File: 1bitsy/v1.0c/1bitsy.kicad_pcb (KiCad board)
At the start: 4 copper layers, 38.1 x 17.8 mm, 105 parts, among them J1 BOOT, P1 CONN_01X01, P10 CONN_01X01, P11 CONN_01X01, P12 CONN_01X01, P13 CONN_01X01, P14 CONN_01X01, P15 CONN_01X01, P16 CONN_01X01, P17 CONN_01X01, P18 CONN_01X01, P19 CONN_01X01, P2 CONN_01X01, P20 CONN_01X01, P21 CONN_01X01, P22 CONN_01X01, P23 CONN_01X01, P24 USB_OTG, P25 CONN_01X01, P26 CONN_01X01, P27 CONN_01X01, P28 CONN_01X01, P29 CONN_01X01, P3 CONN_01X01, P30 CONN_01X01, P31 CONN_01X01, P32 CONN_01X01, P33 CONN_01X01, P34 CONN_01X01, P35 CONN_01X01, P36 CONN_01X01, P37 CONN_01X01, P38 CONN_01X01, P39 CONN_01X01, P4 CONN_01X01, P40 CONN_01X01, P41 CONN_01X01, P42 CONN_01X01, P43 TP, P44 TP, P45 TP, P46 TP, P47 TP, P48 CONN_01X01, P49 CONN_01X01, P5 CONN_01X01, P50 CONN_01X01, P51 CONN_01X01, P52 CONN_01X01, P53 CONN_01X01, P54 CONN_01X01, P55 CONN_01X01, P6 CONN_01X01, P7 CONN_01X01, P8 CONN_01X01, P9 CONN_01X01, SW1 TACT_G, U1 VREG_3V3, U2 STM32F415RGT, X1 32.768kHz, X2 25MHz, X3 JTAG-10

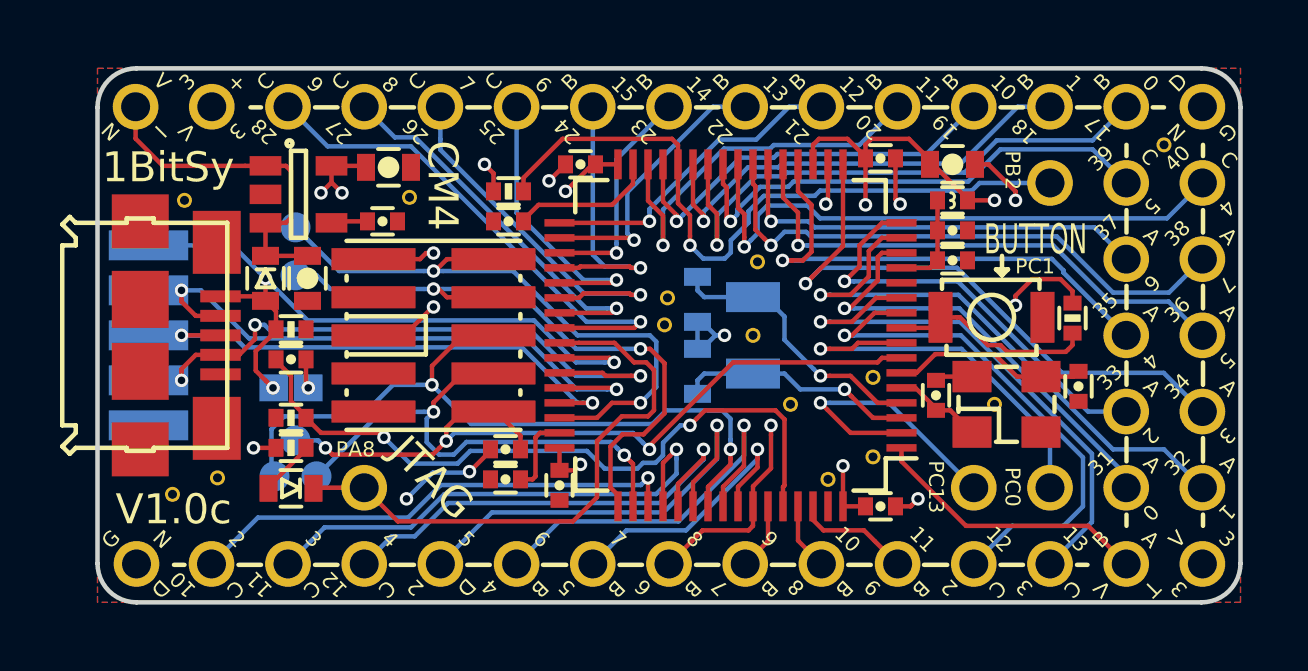
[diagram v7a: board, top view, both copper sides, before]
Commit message: A lot of silkscreen work.
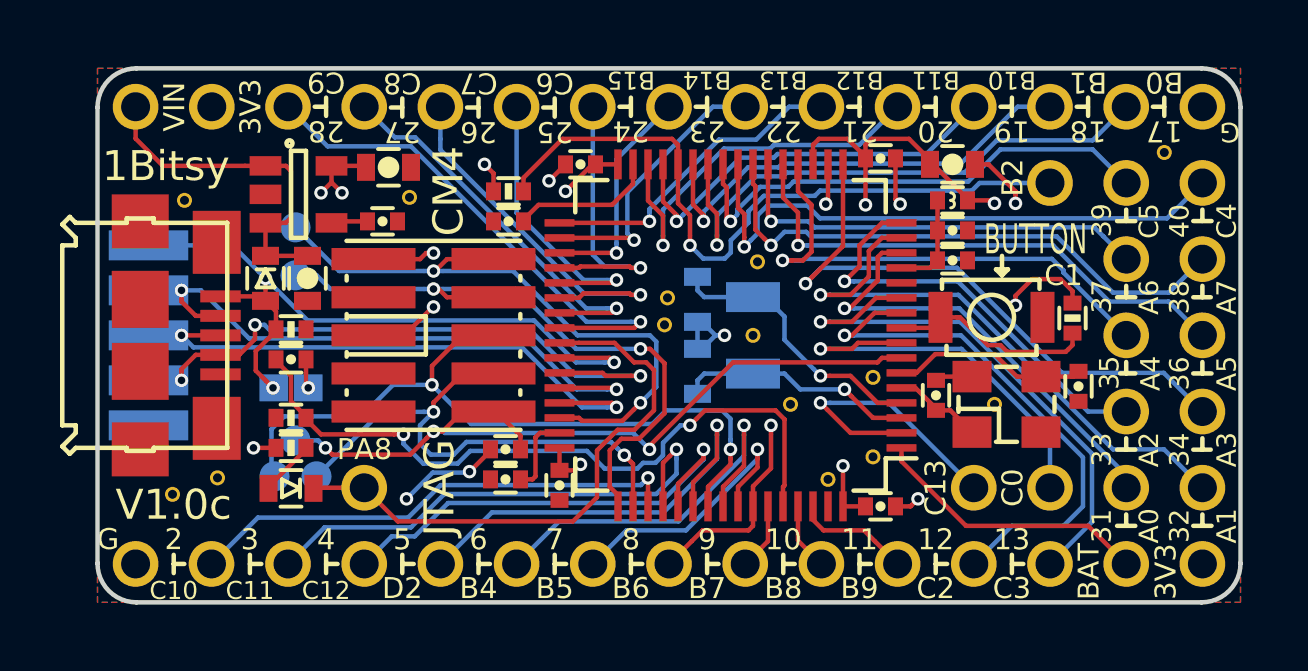
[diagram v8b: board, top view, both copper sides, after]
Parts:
- moved REF** 4.00 mm to (127.8, 45.7), turned to 270 degrees
- moved LOGO1 1.57 mm to (111.9, 45.7), turned to 270 degrees
- moved REF** 0.25 mm to (135.9, 39.6)
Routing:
- net /USB_D+: track 17.0 -> 18.8 mm
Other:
- board text added: "1Bitsy"
- board text added: "A0"
- board text added: "A1"
- board text added: "A2"
- board text added: "A3"
- board text added: "A4"
- board text added: "A5"
- board text added: "A6"
- board text added: "A7"
- board text added: "B0"
- board text added: "B1"
- board text added: "B10"
- board text added: "B11"
- board text added: "B12"
- board text added: "B13"
- board text added: "B14"
- board text added: "B15"
- board text added: "B2"
- board text added: "B4"
- board text added: "B5"
- board text added: "B6"
- board text added: "B7"
- board text added: "B8"
- board text added: "B9"
- board text added: "BAT"
- board text added: "C0"
- board text added: "C1"
- board text added: "C10"
- board text added: "C11"
- board text added: "C12"
- board text added: "C13"
- board text added: "C2"
- board text added: "C3"
- board text added: "C4"
- board text added: "C5"
- board text added: "C6"
- board text added: "C7"
- board text added: "C8"
- board text added: "C9"
- board text added: "D2"
- board text removed: "+"
- board text removed: "0"
- board text removed: "1BitSy"
- board text removed: "A"
- board text removed: "B"
- board text removed: "C"
- board text removed: "D"
- board text removed: "I"
- board text removed: "N"
- board text removed: "PB2"
- board text removed: "PC0"
- board text removed: "PC1"
- board text removed: "PC13"
- board text removed: "T"
- board text removed: "V"
